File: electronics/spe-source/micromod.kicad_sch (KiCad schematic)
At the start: 7 parts, among them IC1 AT24C02C-SSHM, X2 MICROMOD_FUNCTION_BOARD_EDGE

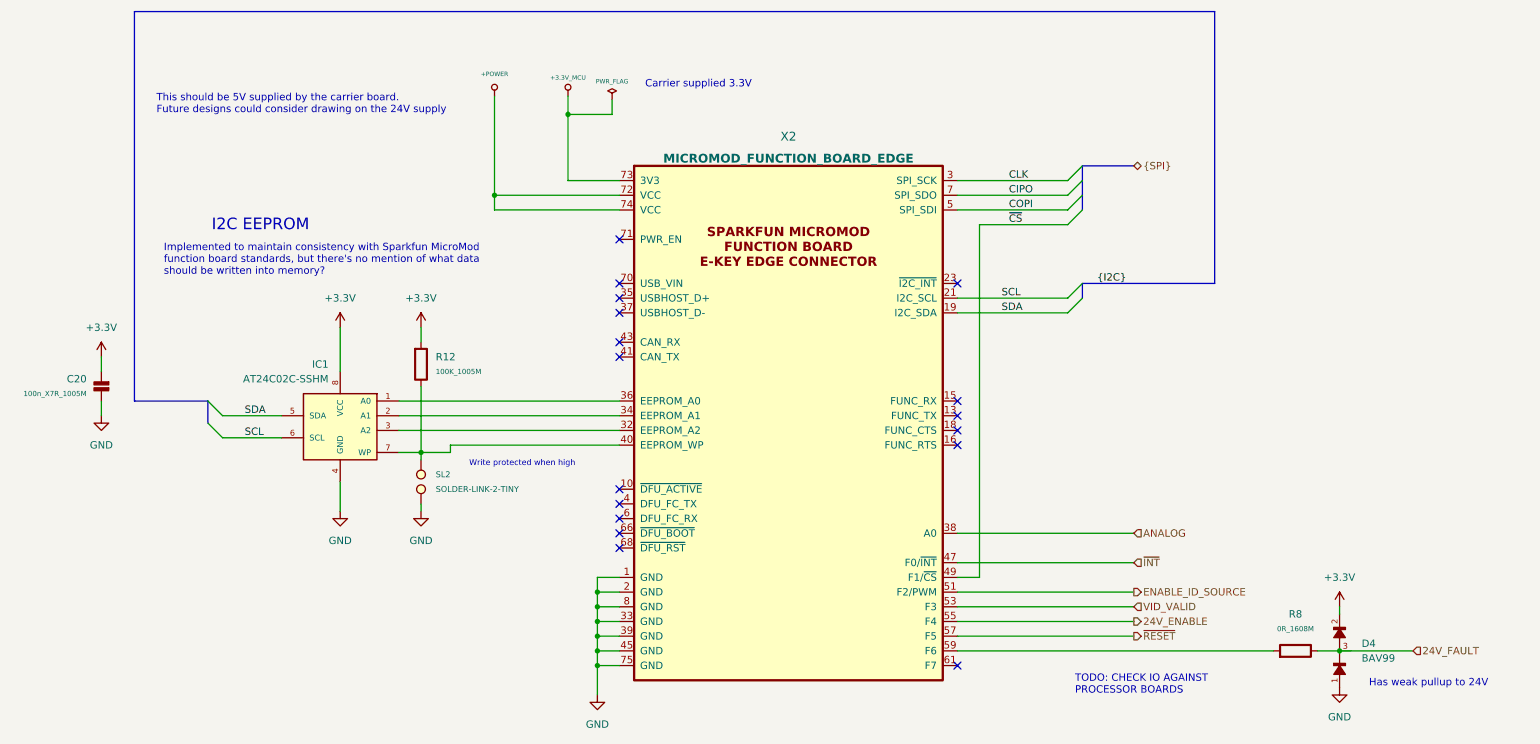
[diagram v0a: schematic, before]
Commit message: PSE routing spaghetti complete
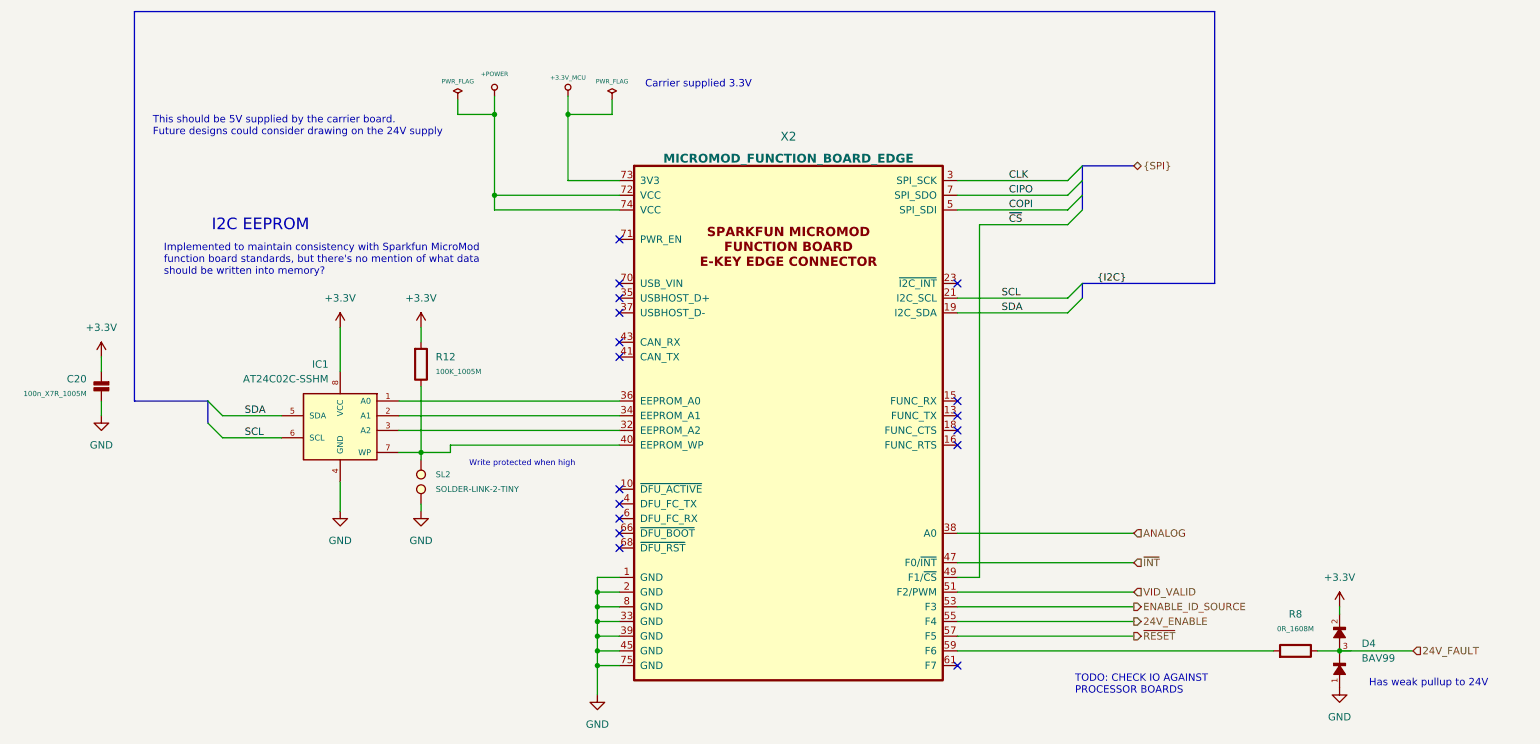
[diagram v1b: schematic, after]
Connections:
- net ENABLE_ID_SOURCE: now also X2.53 (F3); no longer X2.51 (F2/PWM)
- net VID_VALID: now also X2.51 (F2/PWM); no longer X2.53 (F3)
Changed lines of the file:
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@@
   (junction (at 123.19 129.54) (diameter 0) (color 0 0 0 0)
+  )
+  (junction (at 105.41 39.37) (diameter 0) (color 0 0 0 0)
   )
   (junction (at 123.19 134.62) (diameter 0) (color 0 0 0 0)
@@
     (stroke (width 0) (type default))
   )
+  (wire (pts (xy 105.41 39.37) (xy 105.41 53.34))
+    (stroke (width 0) (type default))
+  )
   (wire (pts (xy 92.71 97.79) (xy 92.71 99.06))
     (stroke (width 0) (type default))
@@
     (stroke (width 0) (type default))
   )
+  (wire (pts (xy 99.06 36.83) (xy 99.06 39.37))
+    (stroke (width 0) (type default))
+  )
   (wire (pts (xy 123.19 124.46) (xy 127 124.46))
     (stroke (width 0) (type default))
@@
     (stroke (width 0) (type default))
   )
+  (wire (pts (xy 99.06 39.37) (xy 105.41 39.37))
+    (stroke (width 0) (type default))
+  )
   (wire (pts (xy 78.74 102.87) (xy 78.74 107.95))
     (stroke (width 0) (type default))
@@
     (stroke (width 0) (type default))
   )
+  (wire (pts (xy 105.41 36.195) (xy 105.41 39.37))
+    (stroke (width 0) (type default))
+  )
   (wire (pts (xy 189.23 119.38) (xy 185.42 119.38))
     (stroke (width 0) (type default))
@@
     (stroke (width 0) (type default))
   )
-  (wire (pts (xy 105.41 53.34) (xy 105.41 36.195))
-    (stroke (width 0) (type default))
-  )
   (wire (pts (xy 127 55.88) (xy 105.41 55.88))
     (stroke (width 0) (type default))
@@
   )
   (text "This should be 5V supplied by the carrier board.\nFuture designs could consider drawing on the 24V supply"
-    (at 46.99 39.37 0)
+    (at 46.355 43.18 0)
     (effects (font (size 1.27 1.27)) (justify left bottom))
   )
@@
     (effects (font (size 1.27 1.27)) (justify left))
   )
-  (hierarchical_label "ENABLE_ID_SOURCE" (shape output) (at 215.9 121.92 0) (fields_autoplaced)
-    (effects (font (size 1.27 1.27)) (justify left))
-  )
-  (hierarchical_label "VID_VALID" (shape input) (at 215.9 124.46 0) (fields_autoplaced)
+  (hierarchical_label "ENABLE_ID_SOURCE" (shape output) (at 215.9 124.46 0) (fields_autoplaced)
+    (effects (font (size 1.27 1.27)) (justify left))
+  )
+  (hierarchical_label "VID_VALID" (shape input) (at 215.9 121.92 0) (fields_autoplaced)
     (effects (font (size 1.27 1.27)) (justify left))
   )
@@
         )
       )
+    )
+  )
+  (symbol (lib_id "appli_power:PWR_FLAG") (at 99.06 36.83 0) (unit 1)
+    (in_bom yes) (on_board yes) (dnp no) (fields_autoplaced)
+    (property "Reference" "#FLG03" (at 99.06 35.56 0)
+      (effects (font (size 0.762 0.762)) hide)
+    )
+    (property "Value" "PWR_FLAG" (at 99.06 33.655 0)
+      (effects (font (size 0.762 0.762)))
+    )
+    (property "Footprint" "" (at 99.06 36.83 0)
+      (effects (font (size 1.524 1.524)))
+    )
+    (property "Datasheet" "" (at 99.06 36.83 0)
+      (effects (font (size 1.524 1.524)))
+    )
+    (pin "1")
+    (instances
+      (project "spe-source"
+        (path "/f0a501c7-1ad1-4c59-9255-3d6aa4545d8b/4db035f6-4a09-4a2b-8e2e-a64ccd99d7de"
+          (reference "#FLG03") (unit 1)
+        )
+      )
